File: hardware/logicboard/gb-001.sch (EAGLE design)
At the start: 2 parts

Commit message: Expanded logicboard.
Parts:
- removed SV1: (no value), con-ml:ML16LE
- added SV0: (no value), con-ml:ML34LE
- added SV2: (no value), con-ml:ML20LE
- added SV3: (no value), con-ml:ML14LE
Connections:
- removed net ANLG0R: SV1-3.S
- removed net ANLG1R: SV1-7.S
- removed net ANLG2R: SV1-11.S
- removed net ANLG3R: SV1-15.S
- removed net DTCT0: SV1-2.S
- removed net DTCT1: SV1-6.S
- removed net DTCT2: SV1-10.S
- removed net DTCT3: SV1-14.S
- removed net GND: SV1-1.S, SV1-13.S, SV1-5.S, SV1-9.S
- removed net VCC/2: SV1-12.S, SV1-16.S, SV1-4.S, SV1-8.S

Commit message: Good one.
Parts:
- removed SV2: (no value), con-ml:ML20LE
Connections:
- new net GND: SV0-10.S, SV0-12.S, SV0-14.S, SV0-16.S, SV0-18.S, SV0-2.S, SV0-20.S, SV0-22.S, SV0-24.S, SV0-26.S, SV0-28.S, SV0-30.S, SV0-32.S, SV0-34.S, SV0-4.S, SV0-6.S, SV0-8.S, SV3-5.S
- new net NC: SV0-17.S
- new net T00: SV0-1.S, SV3-1.S
- new net T01: SV0-3.S, SV3-3.S
- new net T02: SV0-5.S, SV3-7.S
- new net T03: SV0-7.S, SV3-9.S
- new net T04: SV0-9.S, SV3-11.S
- new net T05: SV0-11.S, SV3-2.S
- new net T06: SV0-13.S, SV3-4.S
- new net T07: SV0-15.S, SV3-6.S
- new net T08: SV0-19.S, SV3-8.S
- new net T09: SV0-21.S, SV3-10.S
- new net T10: SV0-23.S, SV3-12.S
- new net T11: SV0-25.S, SV3-14.S
- new net T12: SV0-27.S
- new net T13: SV0-29.S
- new net T14: SV0-31.S
- new net T15: SV0-33.S
- new net VT: SV3-13.S
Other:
- moved on the sheet: SV0-11, SV0-12, SV0-13, SV0-14, SV0-15, SV0-16, SV0-17, SV0-18, SV0-19, SV0-20, SV0-21, SV0-22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

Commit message: Added extra pins.
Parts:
- added JP1: (no value), pinhead:PINHD-2X4
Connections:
- net GND: now also JP1.2, JP1.4, JP1.6, JP1.8
- net T12: now also JP1.1
- net T13: now also JP1.3
- net T14: now also JP1.5
- net T15: now also JP1.7
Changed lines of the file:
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@@
 <part name="SUPPLY1" library="supply2" library_urn="urn:adsk.eagle:library:372" deviceset="GND" device=""/>
 <part name="SUPPLY3" library="supply2" library_urn="urn:adsk.eagle:library:372" deviceset="GND" device=""/>
+<part name="JP1" library="pinhead" library_urn="urn:adsk.eagle:library:325" deviceset="PINHD-2X4" device="" package3d_urn="urn:adsk.eagle:package:22461/2"/>
+<part name="SUPPLY2" library="supply2" library_urn="urn:adsk.eagle:library:372" deviceset="GND" device=""/>
 </parts>
 <sheets>
@@
 <attribute name="VALUE" x="20.955" y="52.705" size="1.778" layer="96"/>
 </instance>
-<instance part="SUPPLY3" gate="GND" x="93.98" y="132.08" smashed="yes">
-<attribute name="VALUE" x="92.075" y="128.905" size="1.778" layer="96"/>
+<instance part="SUPPLY3" gate="GND" x="93.98" y="55.88" smashed="yes">
+<attribute name="VALUE" x="92.075" y="52.705" size="1.778" layer="96"/>
+</instance>
+<instance part="JP1" gate="A" x="162.56" y="81.28" smashed="yes">
+<attribute name="NAME" x="156.21" y="89.535" size="1.778" layer="95"/>
+<attribute name="VALUE" x="156.21" y="73.66" size="1.778" layer="96"/>
+</instance>
+<instance part="SUPPLY2" gate="GND" x="177.8" y="55.88" smashed="yes">
+<attribute name="VALUE" x="175.895" y="52.705" size="1.778" layer="96"/>
 </instance>
 </instances>
@@
 <wire x1="104.14" y1="223.52" x2="93.98" y2="223.52" width="0.1524" layer="91"/>
 <pinref part="SUPPLY3" gate="GND" pin="GND"/>
-<wire x1="93.98" y1="223.52" x2="93.98" y2="134.62" width="0.1524" layer="91"/>
+<wire x1="93.98" y1="223.52" x2="93.98" y2="58.42" width="0.1524" layer="91"/>
+</segment>
+<segment>
+<pinref part="JP1" gate="A" pin="2"/>
+<wire x1="167.64" y1="86.36" x2="177.8" y2="86.36" width="0.1524" layer="91"/>
+<wire x1="177.8" y1="86.36" x2="177.8" y2="83.82" width="0.1524" layer="91"/>
+<pinref part="SUPPLY2" gate="GND" pin="GND"/>
+<pinref part="JP1" gate="A" pin="4"/>
+<wire x1="177.8" y1="83.82" x2="177.8" y2="81.28" width="0.1524" layer="91"/>
+<wire x1="177.8" y1="81.28" x2="177.8" y2="78.74" width="0.1524" layer="91"/>
+<wire x1="177.8" y1="78.74" x2="177.8" y2="58.42" width="0.1524" layer="91"/>
+<wire x1="167.64" y1="83.82" x2="177.8" y2="83.82" width="0.1524" layer="91"/>
+<junction x="177.8" y="83.82"/>
+<pinref part="JP1" gate="A" pin="6"/>
+<wire x1="167.64" y1="81.28" x2="177.8" y2="81.28" width="0.1524" layer="91"/>
+<junction x="177.8" y="81.28"/>
+<pinref part="JP1" gate="A" pin="8"/>
+<wire x1="167.64" y1="78.74" x2="177.8" y2="78.74" width="0.1524" layer="91"/>
+<junction x="177.8" y="78.74"/>
 </segment>
 </net>
@@
 <label x="33.02" y="111.76" size="0.8128" layer="95" rot="R180" xref="yes"/>
 </segment>
+<segment>
+<pinref part="JP1" gate="A" pin="1"/>
+<wire x1="160.02" y1="86.36" x2="152.4" y2="86.36" width="0.1524" layer="91"/>
+<label x="152.4" y="86.36" size="0.8128" layer="95" rot="R180" xref="yes"/>
+</segment>
 </net>
 <net name="T13" class="0">
@@
 <label x="33.02" y="101.6" size="0.8128" layer="95" rot="R180" xref="yes"/>
 </segment>
+<segment>
+<pinref part="JP1" gate="A" pin="3"/>
+<wire x1="160.02" y1="83.82" x2="152.4" y2="83.82" width="0.1524" layer="91"/>
+<label x="152.4" y="83.82" size="0.8128" layer="95" rot="R180" xref="yes"/>
+</segment>
 </net>
 <net name="T14" class="0">
@@
 <label x="33.02" y="91.44" size="0.8128" layer="95" rot="R180" xref="yes"/>
 </segment>
+<segment>
+<pinref part="JP1" gate="A" pin="5"/>
+<wire x1="160.02" y1="81.28" x2="152.4" y2="81.28" width="0.1524" layer="91"/>
+<label x="152.4" y="81.28" size="0.8128" layer="95" rot="R180" xref="yes"/>
+</segment>
 </net>
 <net name="T15" class="0">
@@
 <label x="33.02" y="81.28" size="0.8128" layer="95" rot="R180" xref="yes"/>
 </segment>
-</net>
+<segment>
+<pinref part="JP1" gate="A" pin="7"/>
+<wire x1="160.02" y1="78.74" x2="152.4" y2="78.74" width="0.1524" layer="91"/>
+<label x="152.4" y="78.74" size="0.8128" layer="95" rot="R180" xref="yes"/>
+</segment>
+</net>

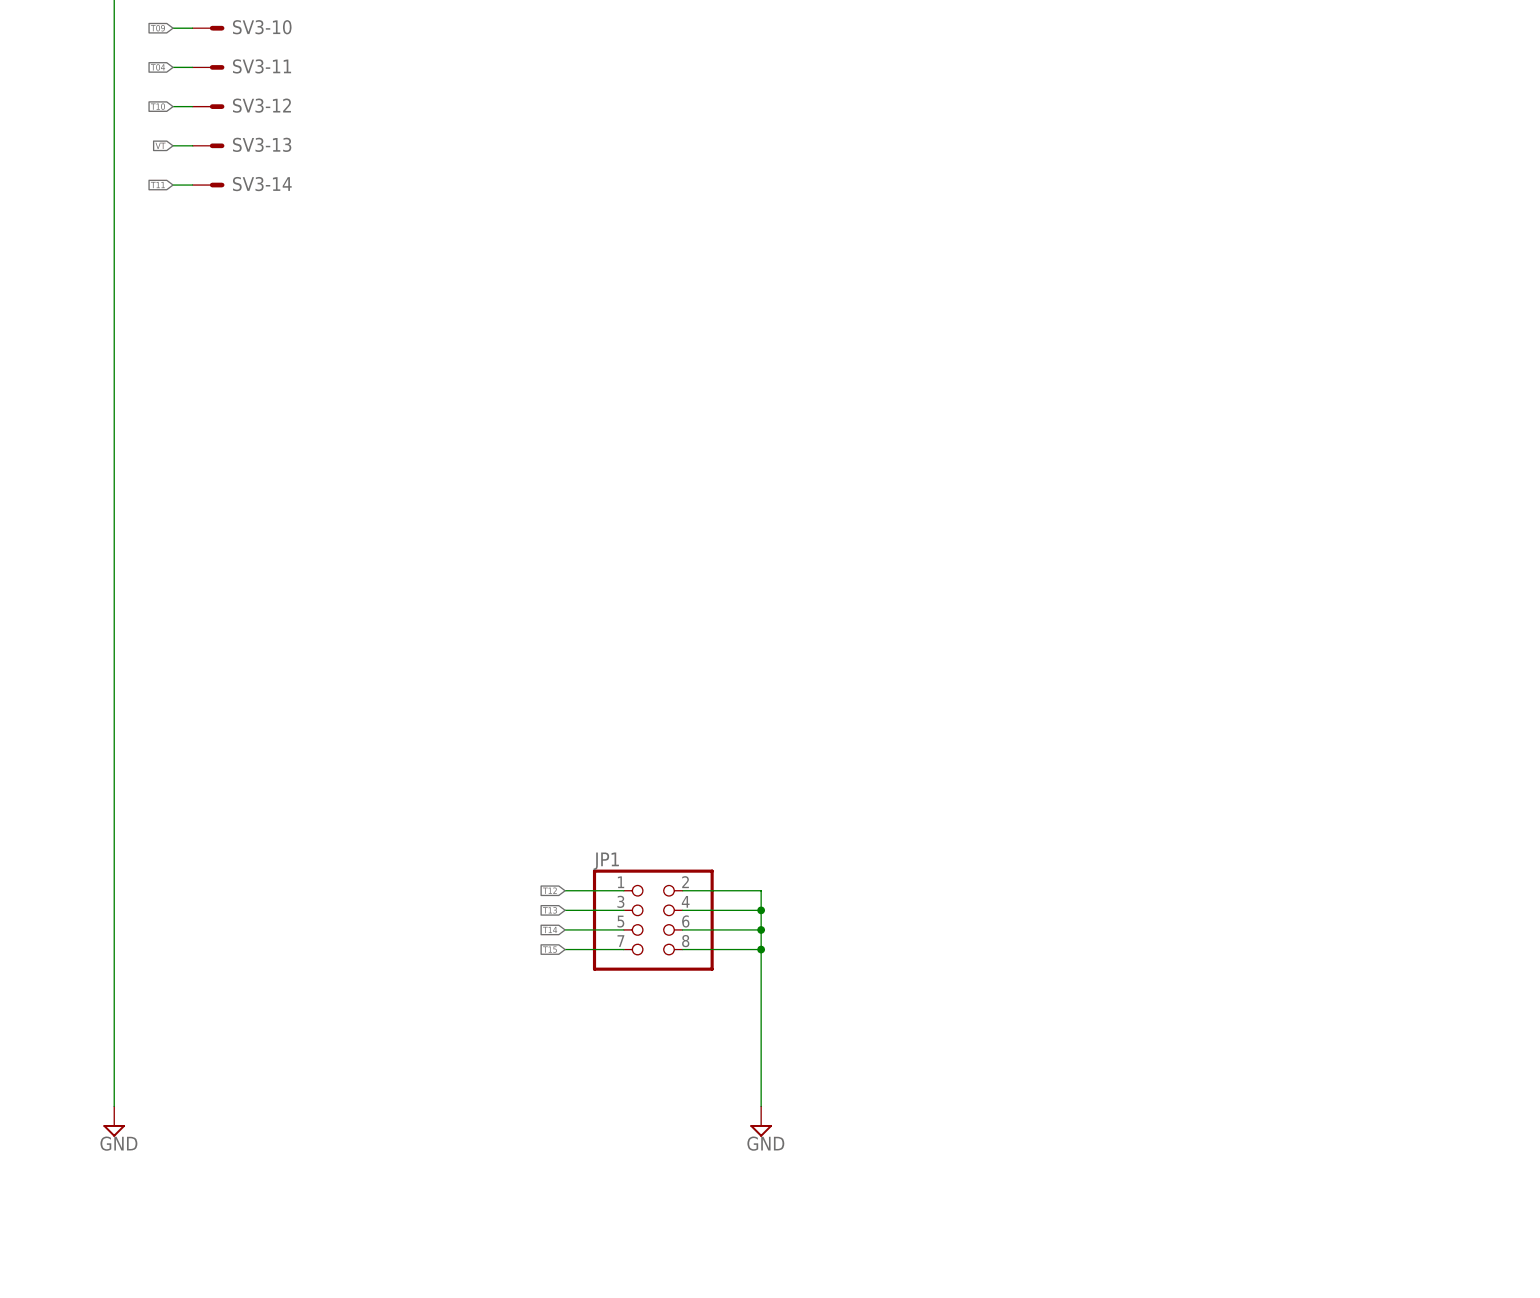
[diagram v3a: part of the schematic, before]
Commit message: Added PWR led.
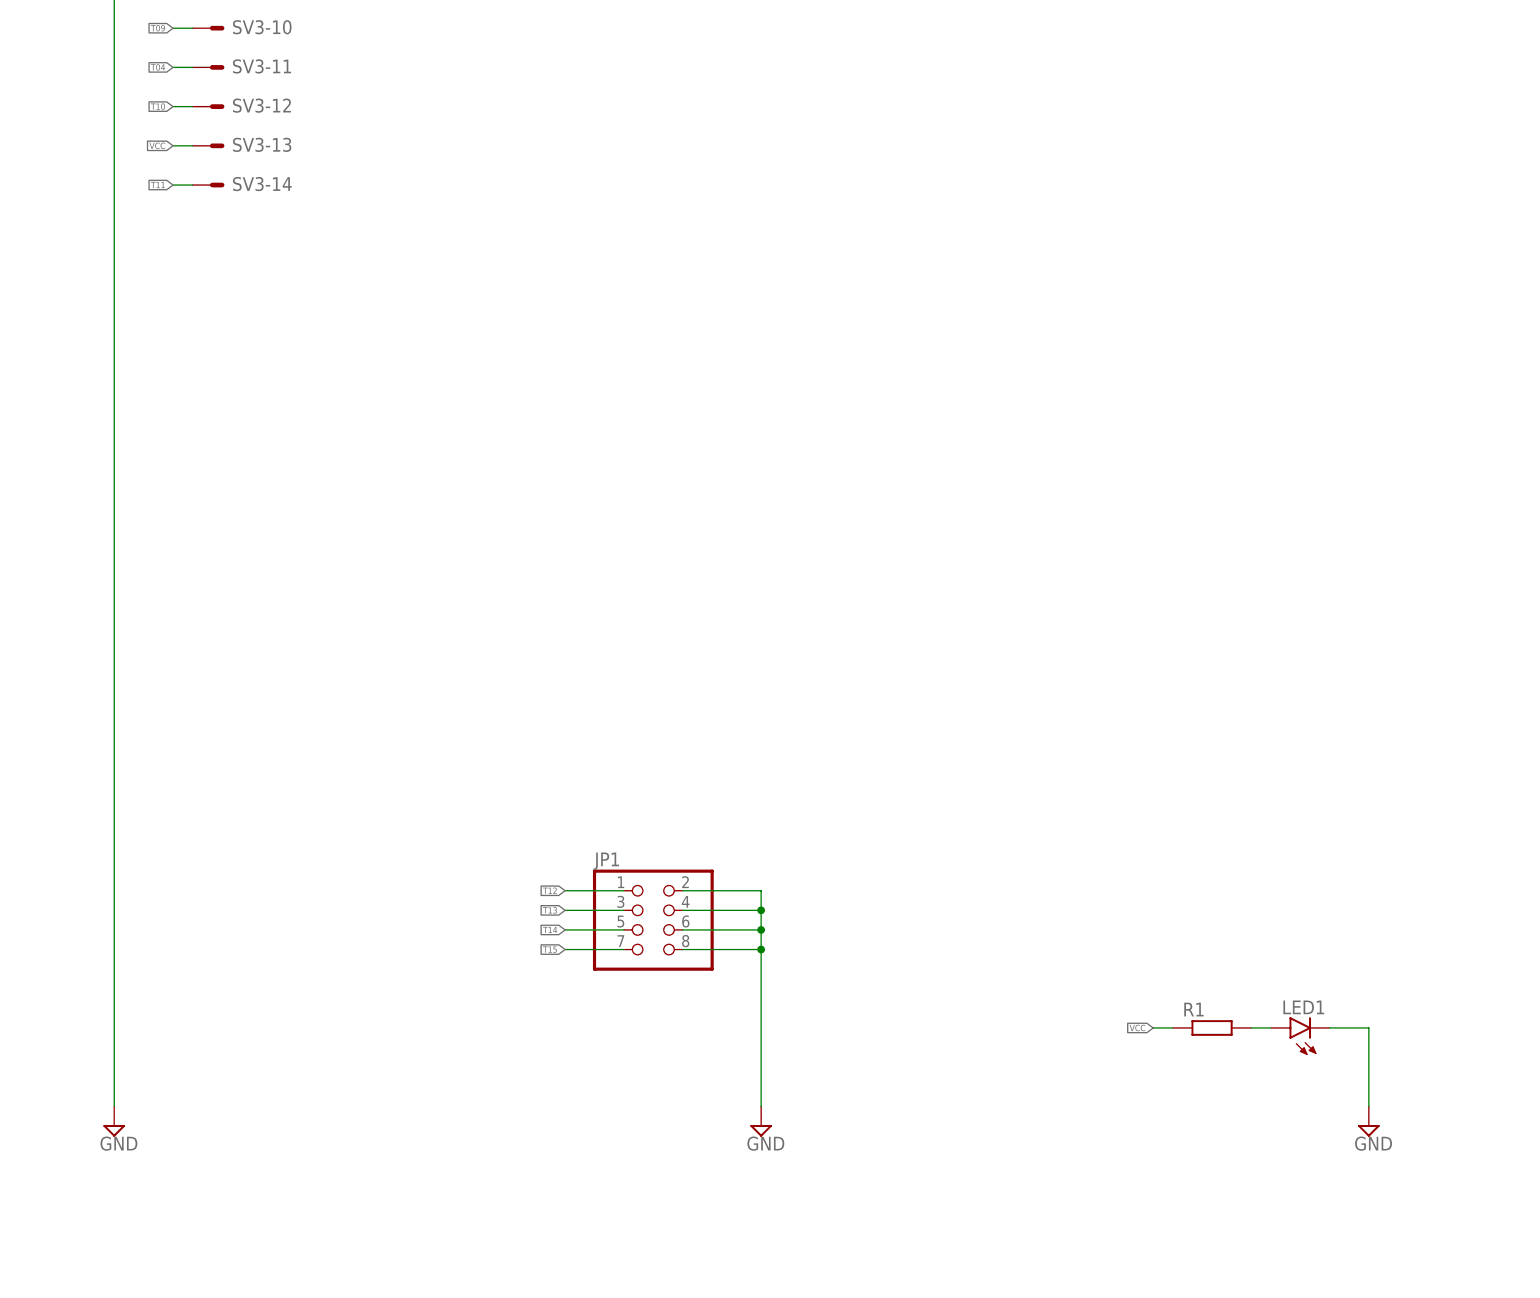
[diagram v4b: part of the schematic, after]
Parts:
- added LED1: (no value), led:LED3MM
- added R1: (no value), rcl:R-EU_0204/5
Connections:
- removed net VT: SV3-13.S
- new net N$2: LED1.A, R1.2
- new net VCC: R1.1, SV3-13.S
- net GND: now also LED1.C
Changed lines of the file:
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@@
 <part name="JP1" library="pinhead" library_urn="urn:adsk.eagle:library:325" deviceset="PINHD-2X4" device="" package3d_urn="urn:adsk.eagle:package:22461/2"/>
 <part name="SUPPLY2" library="supply2" library_urn="urn:adsk.eagle:library:372" deviceset="GND" device=""/>
+<part name="R1" library="rcl" library_urn="urn:adsk.eagle:library:334" deviceset="R-EU_" device="0204/5" package3d_urn="urn:adsk.eagle:package:23488/1"/>
+<part name="LED1" library="led" library_urn="urn:adsk.eagle:library:259" deviceset="LED" device="3MM" package3d_urn="urn:adsk.eagle:package:15797/1"/>
+<part name="SUPPLY4" library="supply2" library_urn="urn:adsk.eagle:library:372" deviceset="GND" device=""/>
 </parts>
 <sheets>
@@
 <instance part="SUPPLY2" gate="GND" x="177.8" y="55.88" smashed="yes">
 <attribute name="VALUE" x="175.895" y="52.705" size="1.778" layer="96"/>
+</instance>
+<instance part="R1" gate="G$1" x="236.22" y="68.58" smashed="yes">
+<attribute name="NAME" x="232.41" y="70.0786" size="1.778" layer="95"/>
+<attribute name="VALUE" x="232.41" y="65.278" size="1.778" layer="96"/>
+</instance>
+<instance part="LED1" gate="G$1" x="246.38" y="68.58" smashed="yes" rot="R90">
+<attribute name="NAME" x="250.952" y="72.136" size="1.778" layer="95" rot="R180"/>
+<attribute name="VALUE" x="250.952" y="74.295" size="1.778" layer="96" rot="R180"/>
+</instance>
+<instance part="SUPPLY4" gate="GND" x="256.54" y="55.88" smashed="yes">
+<attribute name="VALUE" x="254.635" y="52.705" size="1.778" layer="96"/>
 </instance>
 </instances>
@@
 <junction x="177.8" y="78.74"/>
 </segment>
+<segment>
+<pinref part="LED1" gate="G$1" pin="C"/>
+<wire x1="251.46" y1="68.58" x2="256.54" y2="68.58" width="0.1524" layer="91"/>
+<pinref part="SUPPLY4" gate="GND" pin="GND"/>
+<wire x1="256.54" y1="68.58" x2="256.54" y2="58.42" width="0.1524" layer="91"/>
+</segment>
 </net>
 <net name="T00" class="0">
@@
 </segment>
 </net>
-<net name="VT" class="0">
+<net name="VCC" class="0">
 <segment>
 <pinref part="SV3" gate="-13" pin="S"/>
 <wire x1="104.14" y1="182.88" x2="101.6" y2="182.88" width="0.1524" layer="91"/>
 <label x="101.6" y="182.88" size="0.8128" layer="95" rot="R180" xref="yes"/>
+</segment>
+<segment>
+<pinref part="R1" gate="G$1" pin="1"/>
+<wire x1="228.6" y1="68.58" x2="231.14" y2="68.58" width="0.1524" layer="91"/>
+<label x="228.6" y="68.58" size="0.8128" layer="95" rot="R180" xref="yes"/>
+</segment>
+</net>
+<net name="N$2" class="0">
+<segment>
+<pinref part="R1" gate="G$1" pin="2"/>
+<pinref part="LED1" gate="G$1" pin="A"/>
+<wire x1="241.3" y1="68.58" x2="243.84" y2="68.58" width="0.1524" layer="91"/>
 </segment>
 </net>
@@
 packages will not be understood (or retained) with this version.
 </note>
+<note version="8.4" severity="warning">
+Since Version 8.4, EAGLE supports properties for SPICE simulation.
+Probes in schematics and SPICE mapping objects found in parts and library devices
+will not be understood with this version. Update EAGLE to the latest version
+for full support of SPICE simulation.
+</note>
 </compatibility>
